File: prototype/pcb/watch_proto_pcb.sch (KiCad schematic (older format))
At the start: 0 parts

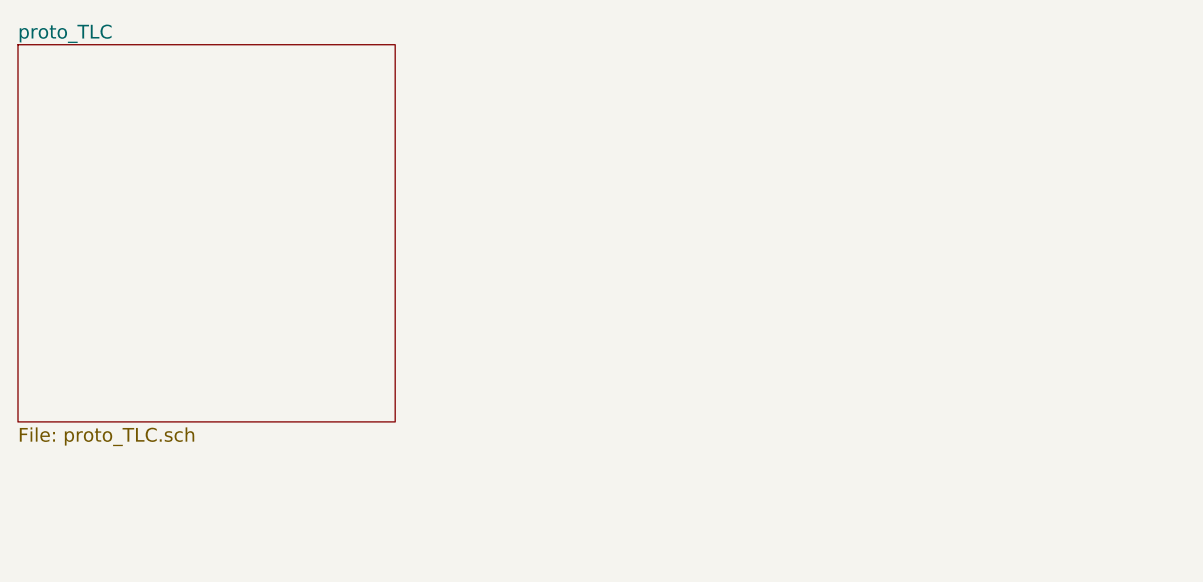
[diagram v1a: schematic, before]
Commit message: Added connectors, power mosfets, hierarchial pins
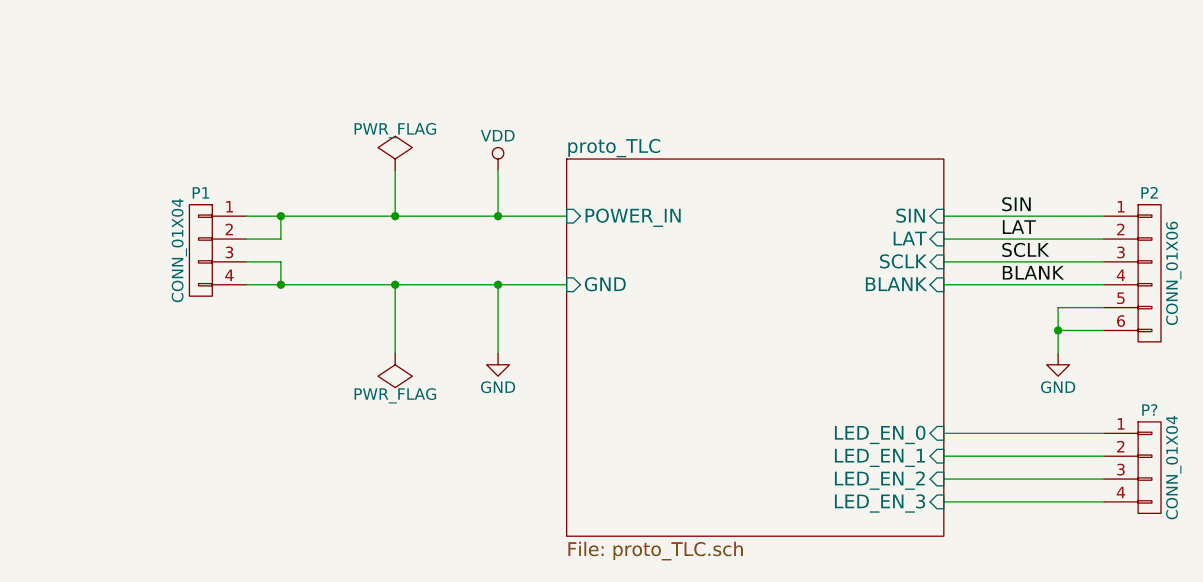
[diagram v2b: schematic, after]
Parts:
- added P1, P?: CONN_01X04, symbol CONN_01X04
- added P2: CONN_01X06, symbol CONN_01X06
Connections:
- new net BLANK: P2.4 (P4)
- new net GND: P1.3 (P3), P1.4 (P4), P2.5 (P5), P2.6 (P6)
- new net LAT: P2.2 (P2)
- new net SCLK: P2.3 (P3)
- new net SIN: P2.1 (P1)
- new net VDD: P1.1 (P1), P1.2 (P2)
- new net proto_TLC/LED_EN_0: P?.1 (P1)
- new net proto_TLC/LED_EN_1: P?.2 (P2)
- new net proto_TLC/LED_EN_2: P?.3 (P3)
- new net proto_TLC/LED_EN_3: P?.4 (P4)
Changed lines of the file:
@@
 LIBS:TLC5954
 LIBS:watch_led
+LIBS:watch_pmos
 LIBS:watch_proto_pcb-cache
 EELAYER 25 0
 EELAYER END
-$Descr B 17000 11000
+$Descr A 11000 8500
 encoding utf-8
 Sheet 1 2
@@
 $EndDescr
 $Sheet
-S 2900 3400 1650 1650
+S 5300 3900 1650 1650
 U 574DFB38
 F0 "proto_TLC" 60
 F1 "proto_TLC.sch" 60
+F2 "SIN" I R 6950 4150 60
+F3 "LAT" I R 6950 4250 60
+F4 "SCLK" I R 6950 4350 60
+F5 "BLANK" I R 6950 4450 60
+F6 "POWER_IN" I L 5300 4150 60
+F7 "GND" I L 5300 4450 60
+F8 "LED_EN_0" I R 6950 5100 60
+F9 "LED_EN_1" I R 6950 5200 60
+F10 "LED_EN_2" I R 6950 5300 60
+F11 "LED_EN_3" I R 6950 5400 60
 $EndSheet
+$Comp
+L CONN_01X04 P1
+U 1 1 574F17B7
+P 3700 4300
+F 0 "P1" H 3700 4550 50  0000 C CNN
+F 1 "CONN_01X04" V 3800 4300 50  0000 C CNN
+F 2 "" H 3700 4300 60  0000 C CNN
+F 3 "" H 3700 4300 60  0000 C CNN
+	1    3700 4300
+	-1   0    0    -1
+$EndComp
+$Comp
+L CONN_01X06 P2
+U 1 1 574F18A7
+P 7850 4400
+F 0 "P2" H 7850 4750 50  0000 C CNN
+F 1 "CONN_01X06" V 7950 4400 50  0000 C CNN
+F 2 "" H 7850 4400 60  0000 C CNN
+F 3 "" H 7850 4400 60  0000 C CNN
+	1    7850 4400
+	1    0    0    -1
+$EndComp
+Wire Wire Line
+	3900 4150 5300 4150
+Wire Wire Line
+	3900 4250 4050 4250
+Wire Wire Line
+	4050 4250 4050 4150
+Connection ~ 4050 4150
+Wire Wire Line
+	4050 4350 3900 4350
+Wire Wire Line
+	3900 4450 5300 4450
+Wire Wire Line
+	4050 4350 4050 4450
+Connection ~ 4050 4450
+Wire Wire Line
+	6950 4150 7650 4150
+Wire Wire Line
+	6950 4250 7650 4250
+Wire Wire Line
+	6950 4350 7650 4350
+Wire Wire Line
+	6950 4450 7650 4450
+$Comp
+L GND #PWR01
+U 1 1 574F1FCF
+P 5000 4750
+F 0 "#PWR01" H 5000 4500 50  0001 C CNN
+F 1 "GND" H 5000 4600 50  0000 C CNN
+F 2 "" H 5000 4750 60  0000 C CNN
+F 3 "" H 5000 4750 60  0000 C CNN
+	1    5000 4750
+	1    0    0    -1
+$EndComp
+$Comp
+L VDD #PWR02
+U 1 1 574F1FF7
+P 5000 3950
+F 0 "#PWR02" H 5000 3800 50  0001 C CNN
+F 1 "VDD" H 5000 4100 50  0000 C CNN
+F 2 "" H 5000 3950 60  0000 C CNN
+F 3 "" H 5000 3950 60  0000 C CNN
+	1    5000 3950
+	1    0    0    -1
+$EndComp
+Wire Wire Line
+	5000 3950 5000 4150
+Connection ~ 5000 4150
+Wire Wire Line
+	5000 4450 5000 4750
+Connection ~ 5000 4450
+$Comp
+L GND #PWR03
+U 1 1 574F20F9
+P 7450 4750
+F 0 "#PWR03" H 7450 4500 50  0001 C CNN
+F 1 "GND" H 7450 4600 50  0000 C CNN
+F 2 "" H 7450 4750 60  0000 C CNN
+F 3 "" H 7450 4750 60  0000 C CNN
+	1    7450 4750
+	1    0    0    -1
+$EndComp
+Wire Wire Line
+	7450 4550 7450 4750
+Wire Wire Line
+	7450 4550 7650 4550
+Wire Wire Line
+	7650 4650 7450 4650
+Connection ~ 7450 4650
+Text Label 7200 4150 0    60   ~ 0
+SIN
+Text Label 7200 4250 0    60   ~ 0
+LAT
+Text Label 7200 4350 0    60   ~ 0
+SCLK
+Text Label 7200 4450 0    60   ~ 0
+BLANK
+$Comp
+L PWR_FLAG #FLG04
+U 1 1 574F2A39
+P 4550 3950
+F 0 "#FLG04" H 4550 4045 50  0001 C CNN
+F 1 "PWR_FLAG" H 4550 4130 50  0000 C CNN
+F 2 "" H 4550 3950 60  0000 C CNN
+F 3 "" H 4550 3950 60  0000 C CNN
+	1    4550 3950
+	1    0    0    -1
+$EndComp
+Wire Wire Line
+	4550 3950 4550 4150
+Connection ~ 4550 4150
+$Comp
+L PWR_FLAG #FLG05
+U 1 1 574F2A91
+P 4550 4750
+F 0 "#FLG05" H 4550 4845 50  0001 C CNN
+F 1 "PWR_FLAG" H 4550 4930 50  0000 C CNN
+F 2 "" H 4550 4750 60  0000 C CNN
+F 3 "" H 4550 4750 60  0000 C CNN
+	1    4550 4750
+	-1   0    0    1
+$EndComp
+Wire Wire Line
+	4550 4750 4550 4450
+Connection ~ 4550 4450
+$Comp
+L CONN_01X04 P?
+U 1 1 574F453F
+P 7850 5250
+F 0 "P?" H 7850 5500 50  0000 C CNN
+F 1 "CONN_01X04" V 7950 5250 50  0000 C CNN
+F 2 "" H 7850 5250 60  0000 C CNN
+F 3 "" H 7850 5250 60  0000 C CNN
+	1    7850 5250
+	1    0    0    -1
+$EndComp
+Wire Wire Line
+	7650 5100 6950 5100
+Wire Wire Line
+	6950 5200 7650 5200
+Wire Wire Line
+	7650 5300 6950 5300
+Wire Wire Line
+	6950 5400 7650 5400
 $EndSCHEMATC

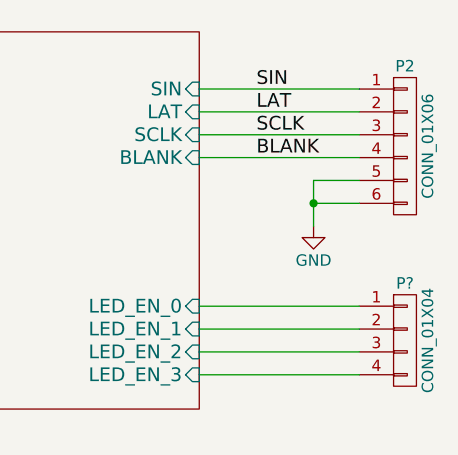
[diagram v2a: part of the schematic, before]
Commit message: Finished footprints and netlist
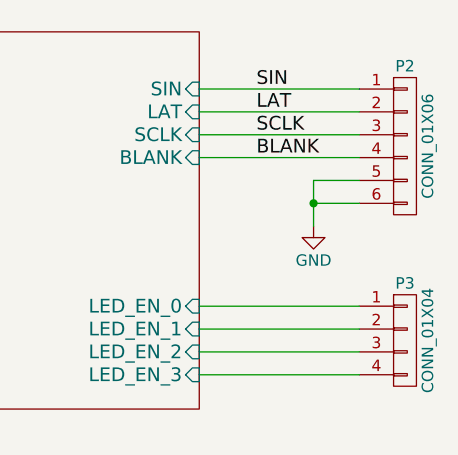
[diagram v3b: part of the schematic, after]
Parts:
- P1: footprint (none) -> Pin_Headers:Pin_Header_Straight_1x04
- P2: footprint (none) -> Pin_Headers:Pin_Header_Straight_1x06
- P3: renamed from P?; footprint (none) -> Pin_Headers:Pin_Header_Straight_1x04
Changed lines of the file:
@@
 F 0 "P1" H 3700 4550 50  0000 C CNN
 F 1 "CONN_01X04" V 3800 4300 50  0000 C CNN
-F 2 "" H 3700 4300 60  0000 C CNN
+F 2 "Pin_Headers:Pin_Header_Straight_1x04" H 3700 4300 60  0001 C CNN
 F 3 "" H 3700 4300 60  0000 C CNN
 	1    3700 4300
@@
 F 0 "P2" H 7850 4750 50  0000 C CNN
 F 1 "CONN_01X06" V 7950 4400 50  0000 C CNN
-F 2 "" H 7850 4400 60  0000 C CNN
+F 2 "Pin_Headers:Pin_Header_Straight_1x06" H 7850 4400 60  0001 C CNN
 F 3 "" H 7850 4400 60  0000 C CNN
 	1    7850 4400
@@
 Connection ~ 4550 4450
 $Comp
-L CONN_01X04 P?
+L CONN_01X04 P3
 U 1 1 574F453F
 P 7850 5250
-F 0 "P?" H 7850 5500 50  0000 C CNN
+F 0 "P3" H 7850 5500 50  0000 C CNN
 F 1 "CONN_01X04" V 7950 5250 50  0000 C CNN
-F 2 "" H 7850 5250 60  0000 C CNN
+F 2 "Pin_Headers:Pin_Header_Straight_1x04" H 7850 5250 60  0001 C CNN
 F 3 "" H 7850 5250 60  0000 C CNN
 	1    7850 5250
